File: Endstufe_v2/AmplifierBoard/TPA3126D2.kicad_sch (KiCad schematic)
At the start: 82 parts, among them J1 Conn_01x01_Pin, J2 Conn_01x01_Pin, J3 banana connector, J4 banana connector, J5 banana connector, J6 banana connector, J7 banana connector, J8 banana connector, U1 TPA3126D2DADR, U2 TPA3126D2DADR

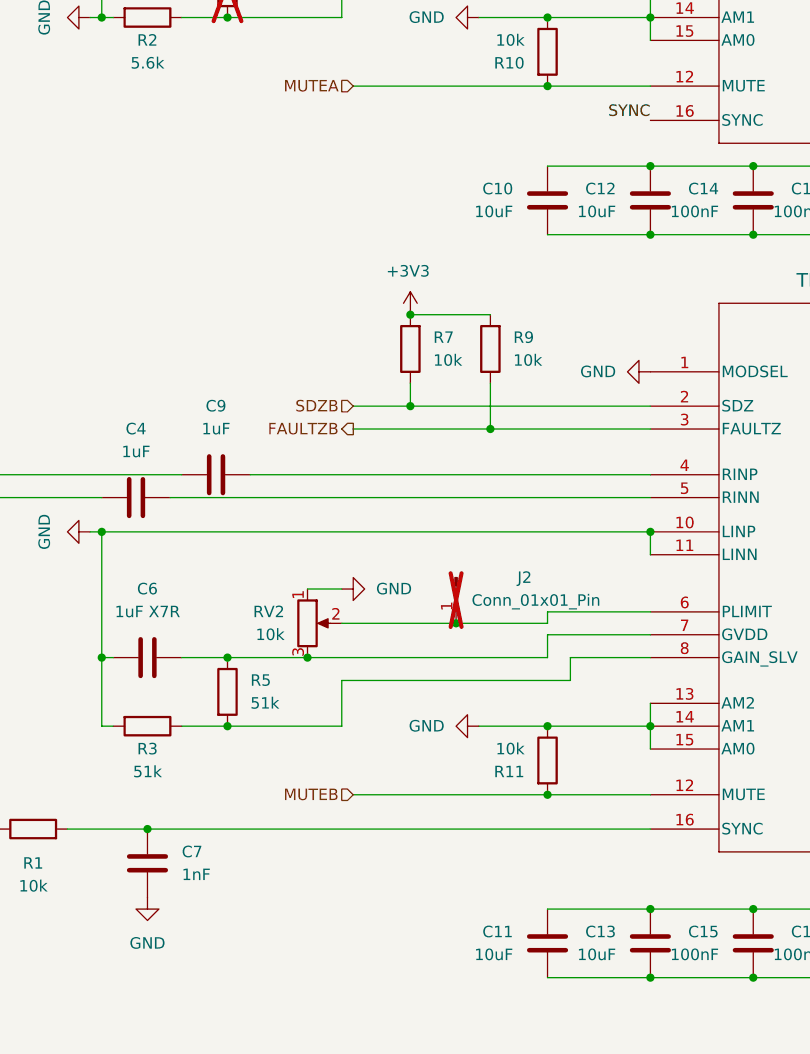
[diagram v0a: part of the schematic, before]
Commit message: Layout amplifier board
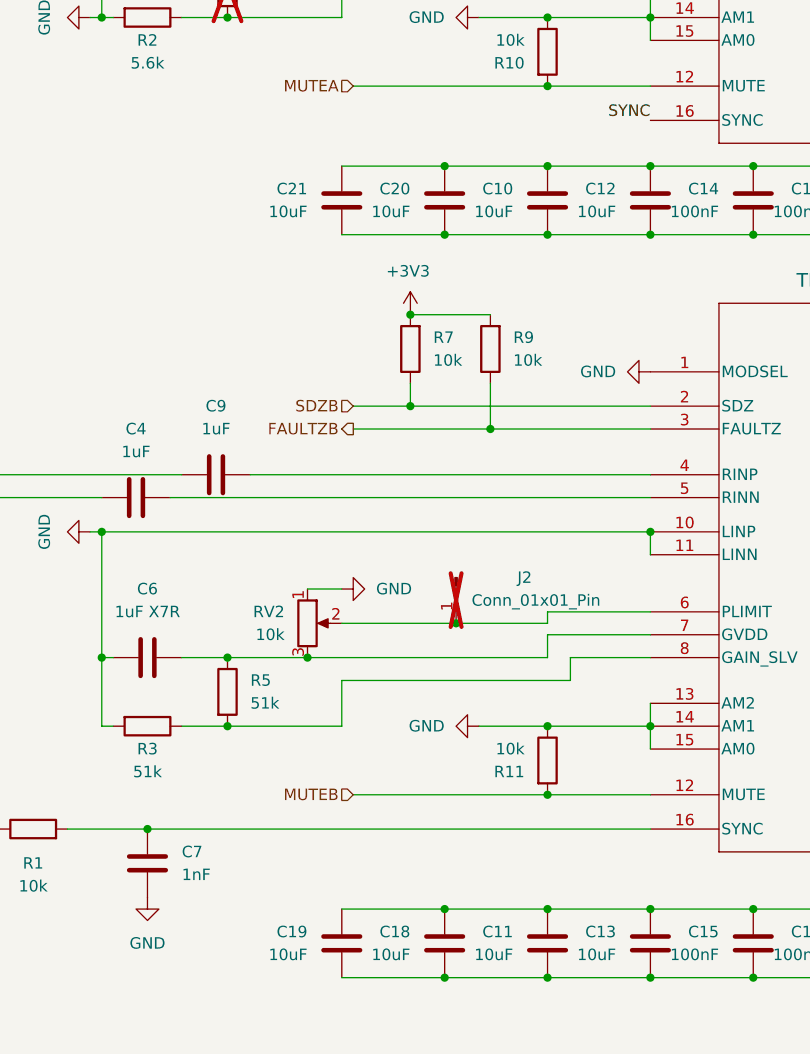
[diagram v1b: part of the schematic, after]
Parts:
- added C18, C19, C20, C21: 10uF, Endstufe:C_1206_3216Metric, symbol Endstufe:C
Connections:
- net +24V: now also C18.1, C19.1, C20.1, C21.1
- net GND: now also C18.2, C19.2, C20.2, C21.2

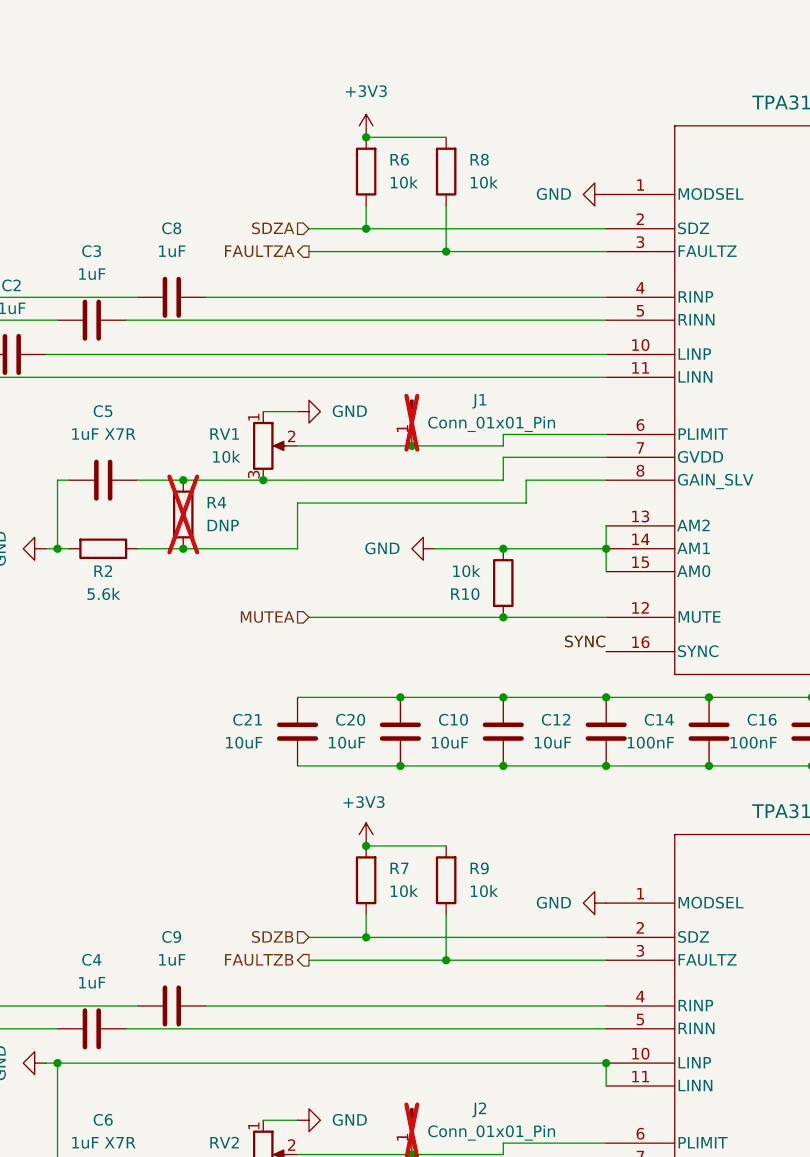
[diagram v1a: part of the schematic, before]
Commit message: Add resistor divider so 24V pull up can be connected to RP2040
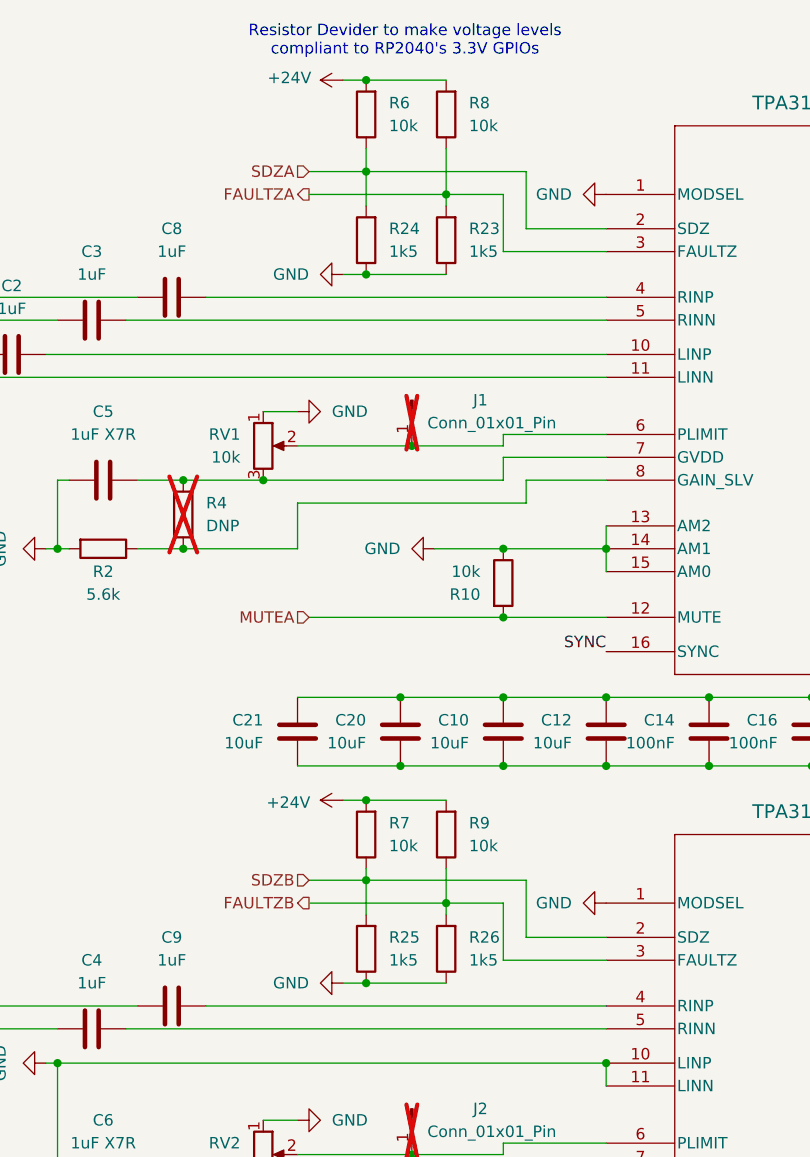
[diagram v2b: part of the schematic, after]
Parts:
- added R23, R24, R25, R26: 1k5, Endstufe:C_0402_1005Metric, symbol Endstufe:R
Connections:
- net +3V3 is gone; now on net +24V: R6.2, R7.2, R8.2, R9.2
- net FAULTZA: now also R23.2
- net FAULTZB: now also R26.2
- net GND: now also R23.1, R24.1, R25.1, R26.1
- net SDZA: now also R24.2
- net SDZB: now also R25.2
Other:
- note added: "Resistor Devider to make voltage levels compliant to RP2040's 3.3V GPIOs"
- moved on the sheet: R6, R7, R8, R9

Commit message: Change unavailable parts to available ones, optimise silkscreen, do via stiching
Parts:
- RV1, RV2: JLCPCB Rotation Offset (none) -> 180
- U1, U2: JLCPCB Rotation Offset (none) -> 90
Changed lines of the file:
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@@
 			)
 		)
+		(property "JLCPCB Rotation Offset" "180"
+			(at 0 127 0)
+			(effects
+				(font
+					(size 1.27 1.27)
+				)
+				(hide yes)
+			)
+		)
 		(pin "1"
 		)
@@
 			)
 		)
+		(property "JLCPCB Rotation Offset" "90"
+			(at 0 228.6 0)
+			(effects
+				(font
+					(size 1.27 1.27)
+				)
+				(hide yes)
+			)
+		)
 		(pin "1"
 		)
@@
 			)
 		)
+		(property "JLCPCB Rotation Offset" "180"
+			(at 0 284.48 0)
+			(effects
+				(font
+					(size 1.27 1.27)
+				)
+				(hide yes)
+			)
+		)
 		(pin "1"
 		)
@@
 			(effects
 				(font
+					(size 1.27 1.27)
+				)
+				(hide yes)
+			)
+		)
+		(property "JLCPCB Rotation Offset" "90"
+			(at 0 71.12 0)
+			(effects
+				(font
